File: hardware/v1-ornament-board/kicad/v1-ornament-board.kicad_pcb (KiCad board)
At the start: 2 copper layers, 75 x 90.1 mm, 249 parts, among them J1 Battery_JST-PH-2.0, SW1 SKRHABE010, U1 XIAO-SAMD21-SMD, U2 74AHCT1G125, U3 MCP73832-2-OT

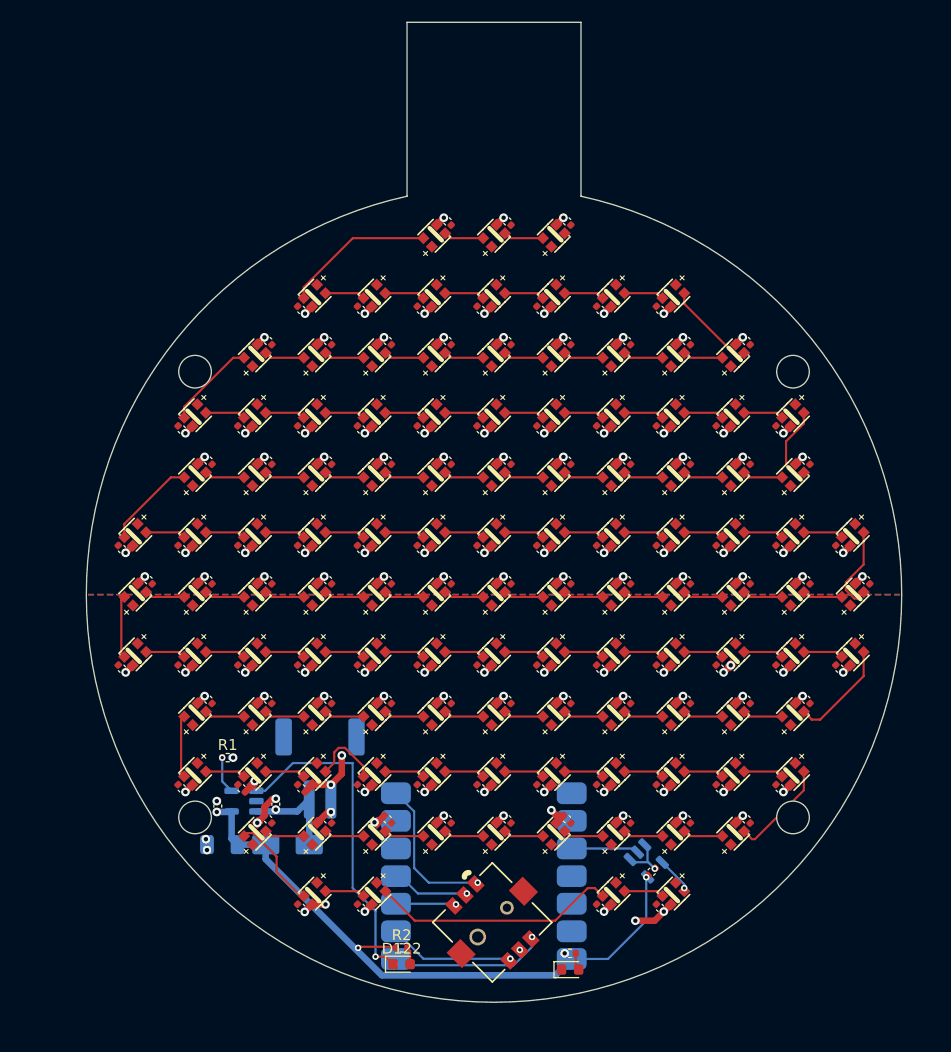
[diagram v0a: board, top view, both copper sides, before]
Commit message: Clean up V1 LED array wiring, decoupling caps, and add tooling holes
- Redraw the WS2812 daisy-chain data connections as explicit wires
  (matching the user's D12-D13-D14 example) instead of floating,
  overlapping labels, for all same-row LED pairs
- Reposition and resize all 118 decoupling caps to Device:C_Small
  using C13 as the template, editing symbols in place so PCB
  footprint links survive (no re-placement needed)
- Add two JLCPCB assembly tooling-hole placeholders (TH1/TH2) per
  their NPTH spec, for the user to position by hand
- Close a 1-micron gap in the decorative tab shape's inner lens
  outline on F.Cu so it forms a valid closed loop for zone fill

Co-Authored-By: Claude Sonnet 5 <noreply@anthropic.com>
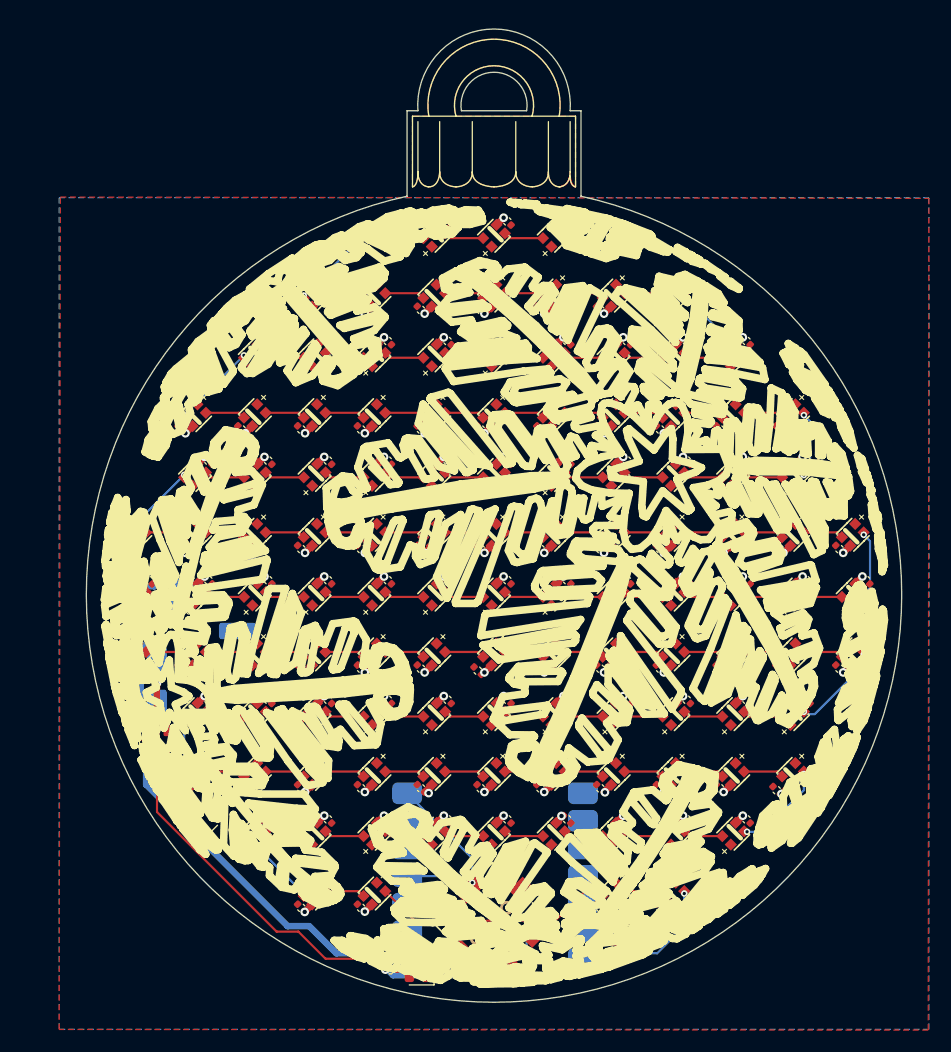
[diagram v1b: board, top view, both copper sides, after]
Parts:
- removed D124: TRIP_LED, LED_SMD:LED_0603_1608Metric
- removed MH1_UR, MH2_UL, MH3_LR, MH4_LL: MountingHole_3mm, MountingHole_3mm
- removed R3: 1k, Resistor_SMD:R_0402_1005Metric
- added TH1: Tooling Hole 1.152mm NPTH, MountingHole_1.152mm, F.Cu at (139.5, 179.5)
- added TH2: Tooling Hole 1.152mm NPTH, MountingHole_1.152mm, F.Cu at (112.0, 115.5)
- D122: value STAT_LED -> KT-0603R
- F1, U2, U3: moved to F.Cu
- R1: value 10k -> 2.49k
- moved D123 19.2 mm to (89.0, 158.0), turned to 90 degrees
- moved J1 19.1 mm to (93.5, 150.0), turned to -90 degrees
- moved C124 14.1 mm to (88.5, 161.0), turned to 0 degrees
- moved U3 9.75 mm to (88.9, 163.5), turned to -90 degrees
- moved R1 9.23 mm to (86.7, 162.2), turned to 90 degrees
- moved U2 7.76 mm to (132.0, 182.0), turned to 0 degrees
- moved C123 6.97 mm to (88.5, 166.1), turned to 0 degrees
- moved C122 6.12 mm to (134.6, 181.6), turned to -90 degrees
- moved F1 2.50 mm to (93.5, 171.0), turned to 45 degrees
- moved R2 2.24 mm to (110.5, 184.5)
- moved D122 1.90 mm to (113.0, 185.2), turned to 180 degrees
- moved U1 1.03 mm to (111.2, 165.4)
- moved C48 0.33 mm to (118.5, 157.0)
- moved C20 0.33 mm to (146.0, 168.0)
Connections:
- J1 pad MP: (no net) -> GND
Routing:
- net GND: track 126.5 -> 114.9 mm, vias 124 -> 125
- net /STAT: track 30.5 -> 39.6 mm, vias 1 -> 0
- net /VBATT: track 9.49 -> 18.2 mm
- net +5V: track 58.9 -> 65.1 mm
- net /LED_DATA_IN: track 6.19 -> 11.1 mm, vias 0 -> 1
- net /LED_DATA_OUT: track 3.49 -> 8.04 mm, vias 1 -> 2
- net /JOY_UP: track 14.0 -> 10.7 mm
- net /LED_CH27: track 6.60 -> 3.68 mm
- net /JOY_LEFT: track 14.4 -> 12.0 mm
- net /LED_CH67: track 8.19 -> 5.98 mm, vias 0 -> 2
- net /LED_CH91: track 7.67 -> 5.98 mm, vias 0 -> 2
- net /TRIP_LED_A: track 1.61 -> 0.00 mm
- net /JOY_SELECT: track 7.18 -> 5.65 mm
- net /JOY_RIGHT: track 11.6 -> 10.0 mm
- net /JOY_DOWN: track 5.55 -> 4.01 mm
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- added copper zone on F.Cu, net (none)
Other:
- board size 75 x 90.1 mm -> 75 x 89.5 mm

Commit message: Move ordering docs to ignored folder; move Emulator to pages, add pixel palette
- Move digikey order/invoice into hardware/v1-ornament-board/ordering-docs/ (gitignored)
- Gitignore KiCad manual pre-edit .bak snapshots and local xmas2026.zip backup
- Rework web emulator: Emulator moves to pages/, adds Pixel/PixelPalette components and virtualHardware
- V1 board fab/KiCad updates (hand-solder BOM, footprint swap script)

Co-Authored-By: Claude Sonnet 5 <noreply@anthropic.com>
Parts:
- removed TH1, TH2: Tooling Hole 1.152mm NPTH, MountingHole_1.152mm
- added D124: TRIP_LED, LED_SMD:LED_0603_1608Metric, F.Cu at (92.5, 186.8)
- added R3: 1k, Resistor_SMD:R_0402_1005Metric, F.Cu at (92.0, 189.1)
- U3: value MCP73832-2-OT -> MCP73832-2-MC; footprint Package_TO_SOT_SMD:SOT-23-5 -> DFN-8-1EP_3x2mm_P0.5mm_EP1.7x1.4mm
- moved J1 41.2 mm to (120.0, 118.5), turned to 180 degrees
- moved D123 39.8 mm to (110.5, 124.5)
- moved C123 10.2 mm to (81.0, 173.0)
- moved R1 9.75 mm to (77.0, 163.0)
- moved U3 9.14 mm to (81.0, 168.0)
- moved C124 8.27 mm to (80.5, 163.0)
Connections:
- J1 pad MP: GND -> (no net)
- SW1 pad 3: /JOY_DOWN -> /JOY_LEFT
- SW1 pad 4: /JOY_LEFT -> /JOY_RIGHT
- SW1 pad 6: /JOY_RIGHT -> /JOY_DOWN
- U1 pad 1: /JOY_LEFT -> /JOY_RIGHT
- U1 pad 2: /JOY_RIGHT -> /JOY_DOWN
- U1 pad 3: /JOY_DOWN -> /JOY_LEFT
- U1 pad 5: unconnected-(U1-D4-Pad5) -> /JOY_UP
- U1 pad 7: /JOY_UP -> unconnected-(U1-D6-Pad7)
- U3 pad 1: /STAT -> +5V
- U3 pad 2: GND -> +5V
- U3 pad 4: +5V -> /VBATT
- U3 pad 5: /PROG -> /STAT
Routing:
- net +5V: track 65.1 -> 7.72 mm, vias 4 -> 2
- net /STAT: track 39.6 -> 0.00 mm
- net /VBATT: track 18.2 -> 0.00 mm, vias 1 -> 0
- net /JOY_LEFT: track 12.0 -> 4.01 mm
- net /JOY_DOWN: track 4.01 -> 10.0 mm
- net GND: track 114.9 -> 109.0 mm, vias 125 -> 120
- net /PROG: track 4.00 -> 0.00 mm
- net /JOY_UP: track 10.7 -> 7.66 mm
- net /JOY_RIGHT: track 10.0 -> 12.0 mm
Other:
- board text added: "(-)"
- board text added: "+"
- board text added: "+5V"
- board text added: "Down"
- board text added: "Ground"
- board text added: "LED Data"
- board text added: "Left"
- board text added: "Right"
- board text added: "Select"
- board text added: "Up"
